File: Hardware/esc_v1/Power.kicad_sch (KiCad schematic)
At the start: 19 parts, among them U1 AZ1117CH-5.0TRG1, U2 AZ1117CH-3.3TRG1, U3 TPS5450DDAR

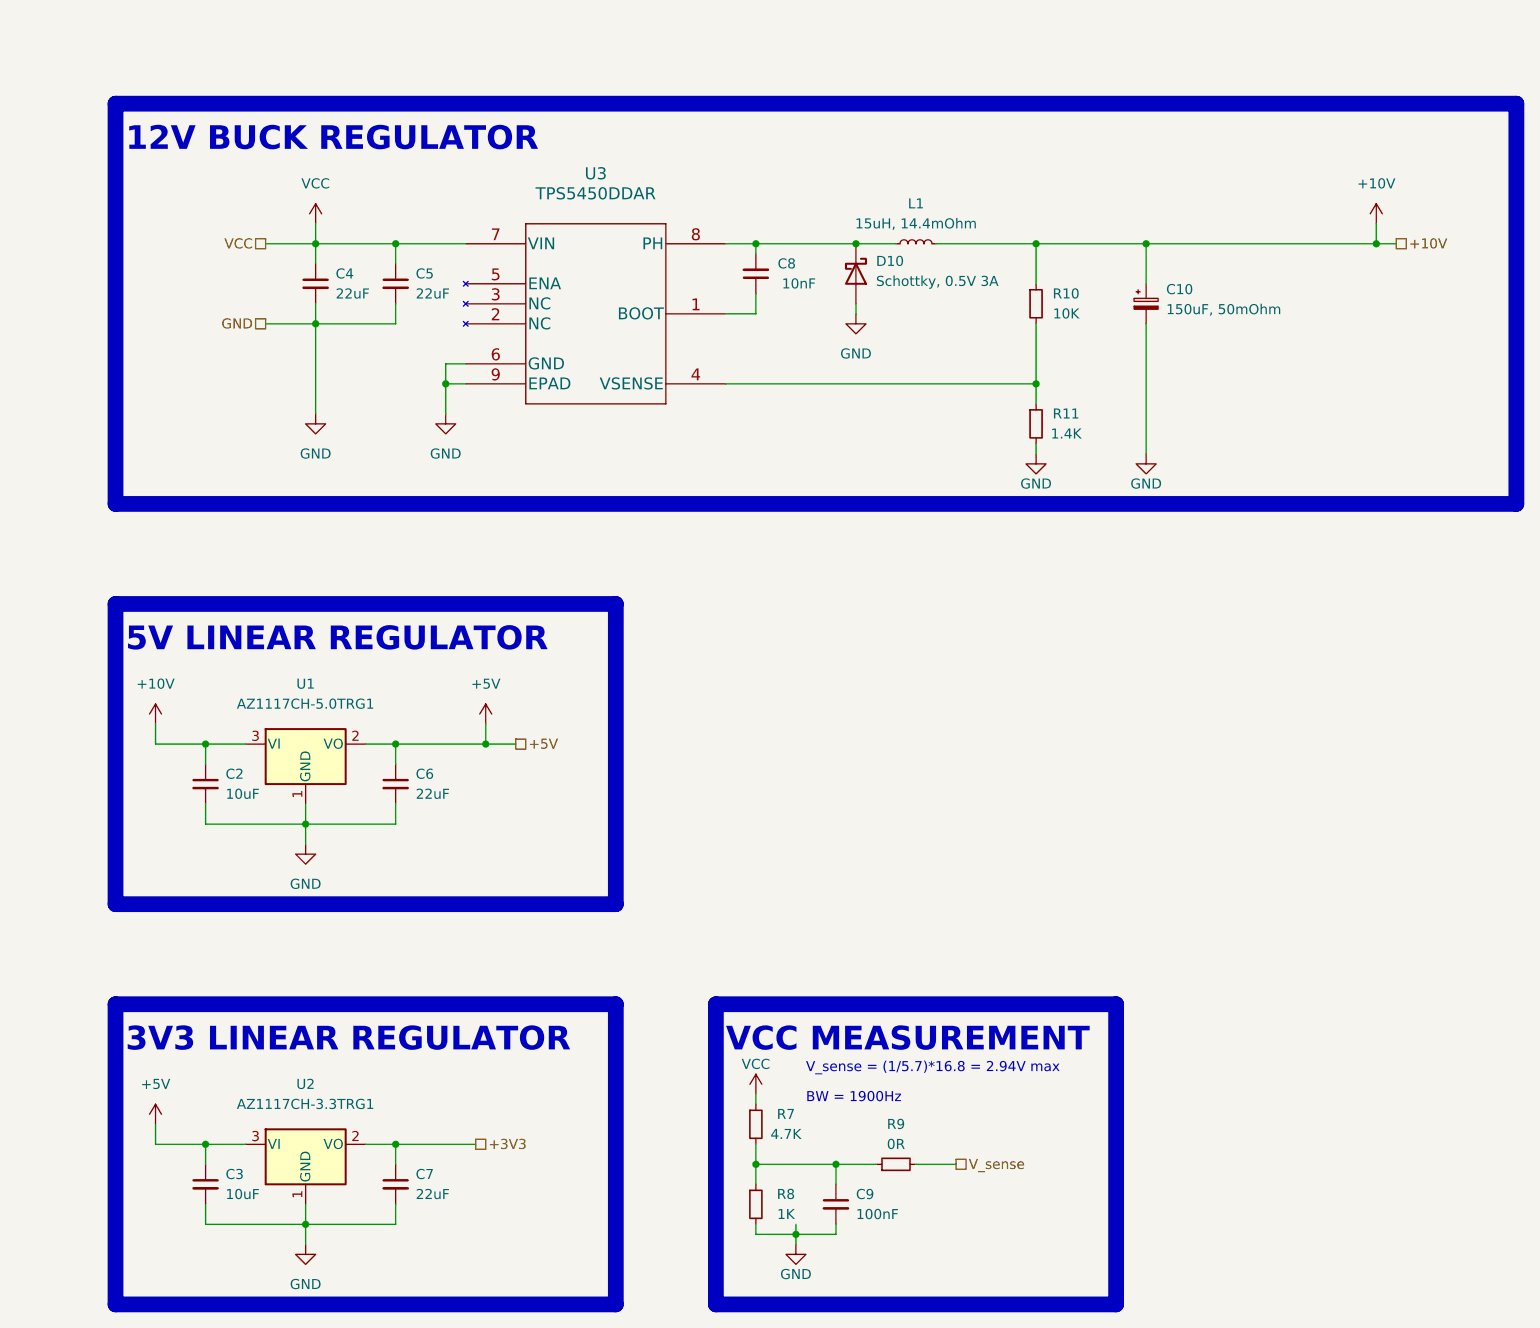
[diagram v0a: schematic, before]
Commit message: changed gate driver, removed 10V buck and 5V LDO, added 5V buck. Started on Layout
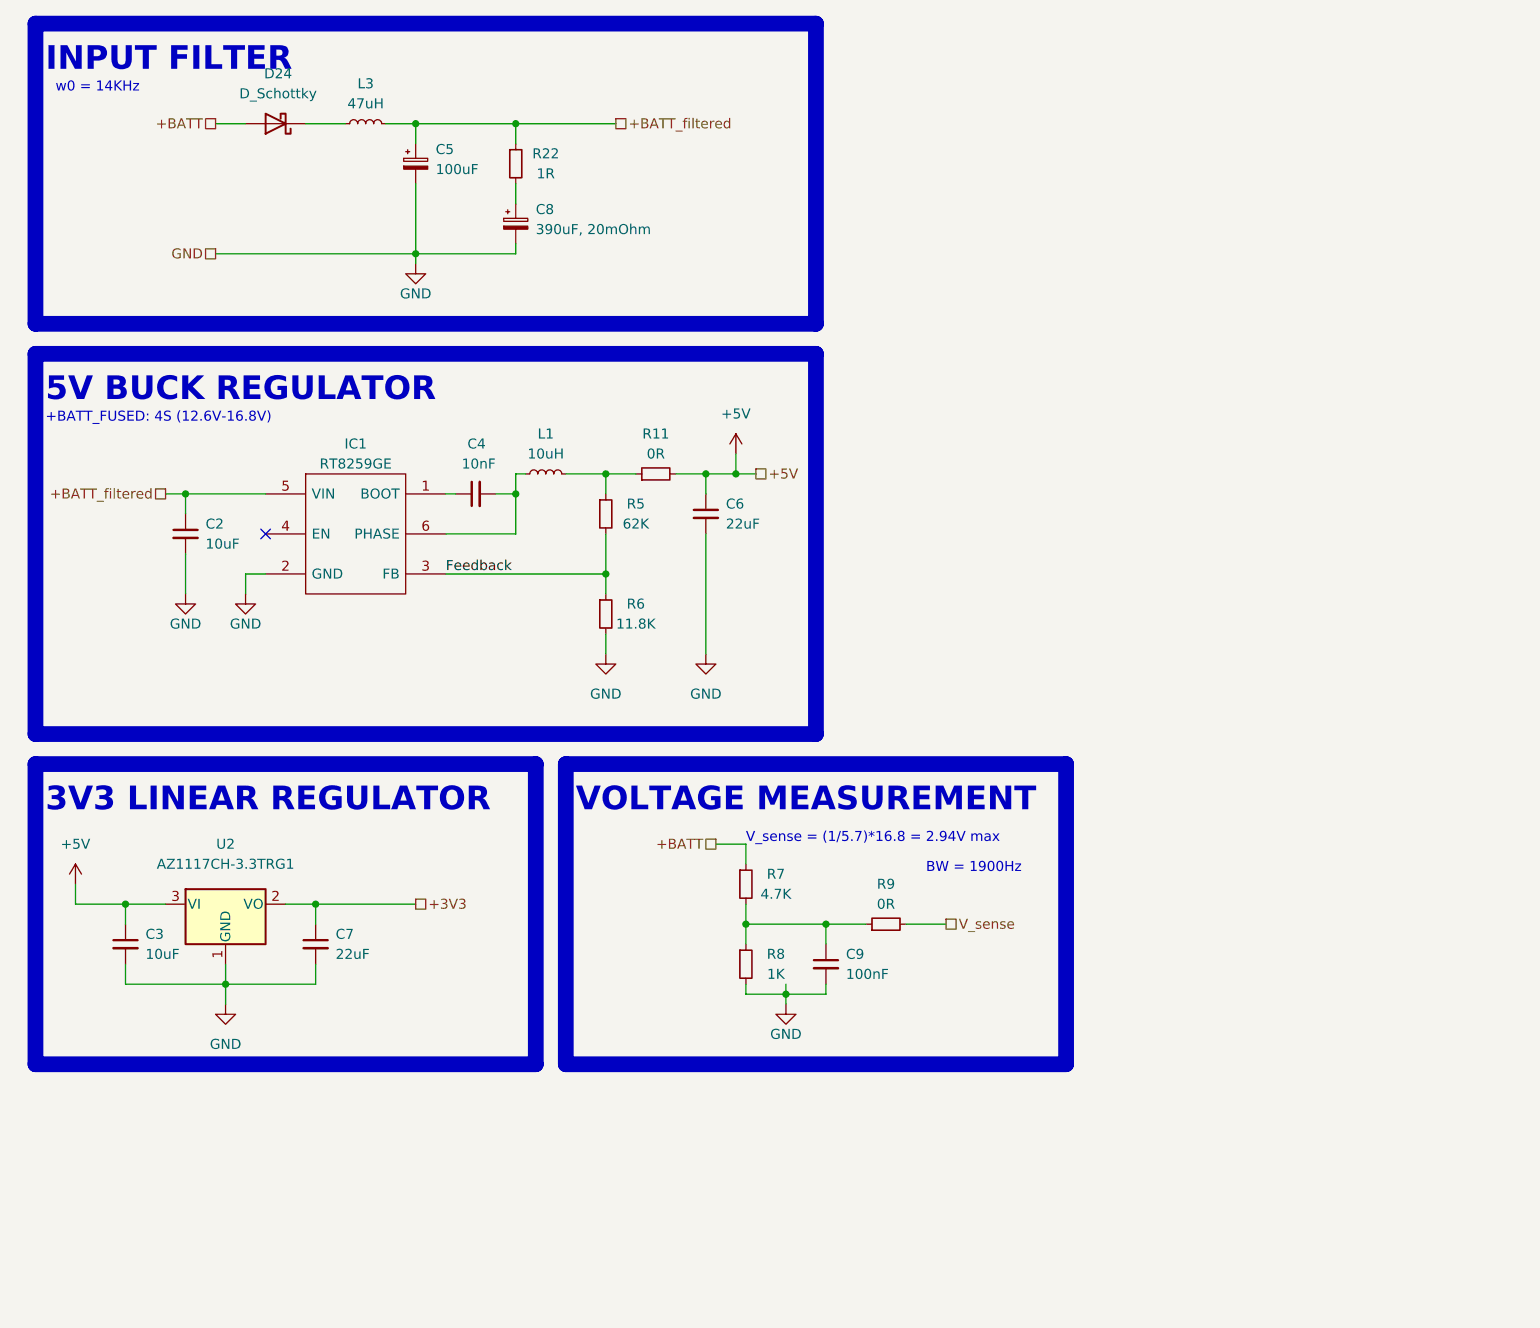
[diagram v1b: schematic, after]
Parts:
- removed C10: 150uF, 50mOhm, T510E107M025ATE050:T510E107M025AT E050, symbol Device:C_Polarized_Small
- removed C5: 22uF, Capacitor_SMD:C_0603_1608Metric, symbol Device:C_Small
- removed C8: 10nF, Capacitor_SMD:C_0603_1608Metric, symbol Device:C_Small
- removed D10: Schottky, 0.5V 3A, Diode_SMD:D_SMA, symbol Device:D_Schottky
- removed R10: 10K, Resistor_SMD:R_0603_1608Metric, symbol Device:R_Small
- removed U1: AZ1117CH-5.0TRG1, Package_TO_SOT_SMD:SOT-223-3_TabPin2, symbol Regulator_Linear:AZ1117-3.3
- removed U3: TPS5450DDAR, Package_SO:TI_SO-PowerPAD-8, symbol TPS5450:TPS5450DDAR
- added C5: 100uF, T510E107M025ATE050:T510E107M025AT E050, symbol Device:C_Polarized_Small
- added C8: 390uF, 20mOhm, Capacitor_SMD:C_Elec_8x10.2, symbol Device:C_Polarized_Small
- added D24: D_Schottky, Diode_SMD:D_SOD-123, symbol Device:D_Schottky
- added IC1: RT8259GE, Package_TO_SOT_SMD:SOT-23-6, symbol RT8259GE:RT8259GE
- added L3: 47uH, SRP1265A-470M:SRP1265A, symbol Device:L_Small
- added R22: 1R, Resistor_SMD:R_0603_1608Metric, symbol Device:R_Small
- added R5: 62K, Resistor_SMD:R_0603_1608Metric, symbol Device:R_Small
- added R6: 11.8K, Resistor_SMD:R_0603_1608Metric, symbol Device:R_Small
- C4: value 22uF -> 10nF
- C6, C7: footprint Capacitor_SMD:C_0603_1608Metric -> Capacitor_SMD:C_0805_2012Metric
- L1: value 15uH, 14.4mOhm -> 10uH; footprint IHLP6767GZER150M11:INDPM172172X700N -> 744025100:Wuerth_Elektronik-744025100-Manufacturer_Recommended; Part No IHLP6767GZER150M11 -> 744025100; Producer Vishay Dale -> Würth Elektronik
- R11: value 1.4K -> 0R
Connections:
- net +5V: now also R11.2
- net GND: now also C5.2, C8.2, IC1.2 (GND), R6.2; no longer C4.2, R11.2
- net at L1.1: now also C4.2, IC1.6 (PHASE)
- net at R11.1: now also L1.2, R5.1
- net +10V renamed +BATT_filtered
- net +BATT_filtered: now also C5.1, IC1.5 (VIN), L3.2, R22.1; no longer L1.2
- net VCC: no longer names the net of C4.1
- net VCC: now also IC1.1 (BOOT); no longer R7.1
- new net: D24.1 (K), L3.1
- new net: C8.1, R22.2
- new net +BATT: D24.2 (A), R7.1
- new net Feedback: IC1.3 (FB), R5.2, R6.1
- no-connect marks 0 -> 1
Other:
- note added: "+BATT_FUSED: 4S (12.6V-16.8V)"
- note added: "5V BUCK REGULATOR"
- note added: "INPUT FILTER"
- note added: "VOLTAGE MEASUREMENT"
- note added: "w0 = 14KHz"
- note removed: "12V BUCK REGULATOR"
- note removed: "5V LINEAR REGULATOR"
- note removed: "VCC MEASUREMENT"
- moved on the sheet: C3, C7, C9, R7, R8, R9, U2

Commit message: Continued on layout
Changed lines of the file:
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@@
     (pin "2")
   )
-  (symbol (lib_id "Device:C_Small") (at 26.67 132.08 0) (unit 1)
+  (symbol (lib_id "Device:C_Small") (at 26.67 132.08 0) (mirror y) (unit 1)
     (in_bom yes) (on_board yes)
-    (property "Reference" "C3" (id 0) (at 29.21 130.8162 0)
+    (property "Reference" "C3" (id 0) (at 24.13 130.8162 0)
       (effects (font (size 1.27 1.27)) (justify left))
     )
-    (property "Value" "10uF" (id 1) (at 29.21 133.3562 0)
+    (property "Value" "10uF" (id 1) (at 24.13 133.3562 0)
       (effects (font (size 1.27 1.27)) (justify left))
     )

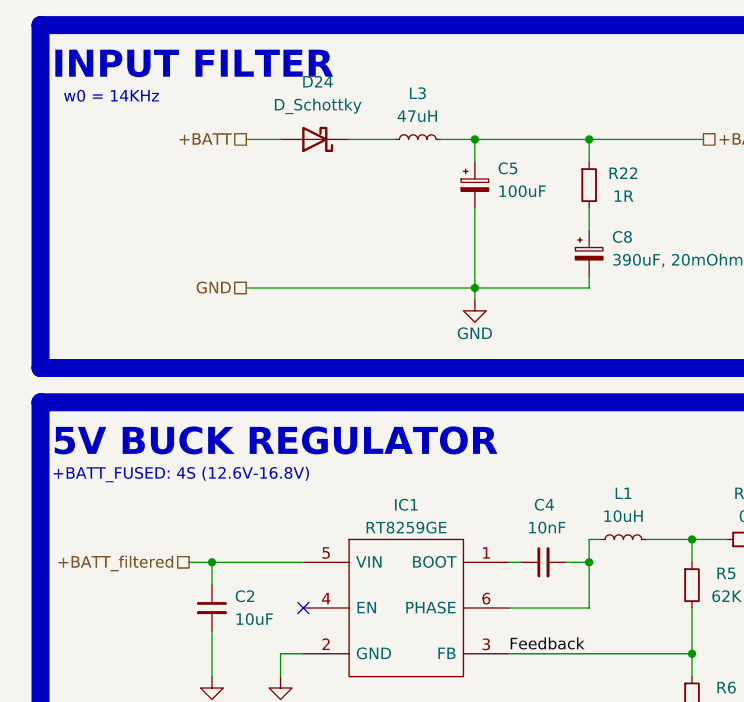
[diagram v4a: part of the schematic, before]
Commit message: Removed USB to serial chip and added serial connector. Finished layout, made production files and sent to production
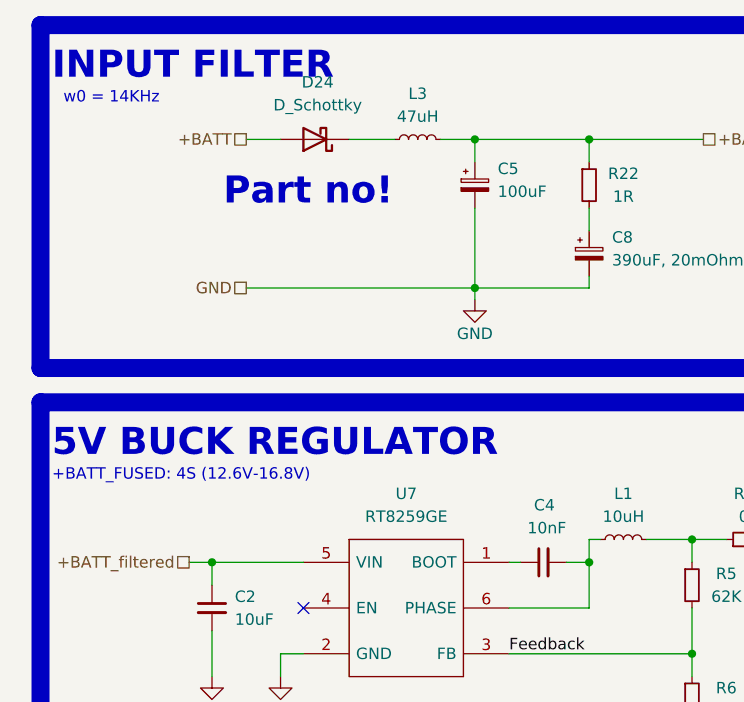
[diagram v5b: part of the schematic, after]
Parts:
- C5: Part no (none) -> T510E107M025ATE050; PartNo T510E107M025ATE050 -> (none)
- C8: Part no (none) -> APXG200ARA391MHA0G; PartNo APXG200ARA391MHA0G -> (none)
- D24: Io 1.5A -> 2A; Part no (none) -> MBR260HW; Producer (none) -> SMC Diode Solutions; Voltage rating 50V -> 60V
- L1: Manufacturer_Name (none) -> Würth Elektronik; Part No 744025100 -> (none); Part no (none) -> 744025100; Producer Würth Elektronik -> (none)
- L3: Manufacturer_Name (none) -> Bourns Inc.; Part No SRP1265A-470M -> (none); Part no (none) -> SRP1265A-470M; Producer Bourns Inc. -> (none)
- U2: Part no (none) -> AZ1117CH-3.3TRG1
- U7: renamed from IC1; Manufacturer_Part_Number RT8259GE -> (none); Part no (none) -> RT8259GE
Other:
- note added: "Part no!"
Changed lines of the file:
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@@
     (effects (font (size 1.27 1.27)) (justify left bottom))
+  )
+  (text "Part no!" (at 35.56 35.56 0)
+    (effects (font (size 3 3) (thickness 0.6) bold) (justify left bottom))
   )
   (text "5V BUCK REGULATOR" (at 16.51 63.5 0)
@@
       (effects (font (size 1.27 1.27)) hide)
     )
-    (property "Part no" "" (id 4) (at 45.72 27.94 90)
-      (effects (font (size 1.27 1.27)) hide)
-    )
-    (property "Producer" "" (id 5) (at 45.72 27.94 90)
-      (effects (font (size 1.27 1.27)) hide)
-    )
-    (property "Voltage rating" "50V" (id 6) (at 45.72 27.94 0)
-      (effects (font (size 1.27 1.27)) hide)
-    )
-    (property "Io" "1.5A" (id 7) (at 45.72 27.94 0)
+    (property "Part no" "MBR260HW" (id 4) (at 45.72 27.94 90)
+      (effects (font (size 1.27 1.27)) hide)
+    )
+    (property "Producer" "SMC Diode Solutions" (id 5) (at 45.72 27.94 90)
+      (effects (font (size 1.27 1.27)) hide)
+    )
+    (property "Voltage rating" "60V" (id 6) (at 45.72 27.94 0)
+      (effects (font (size 1.27 1.27)) hide)
+    )
+    (property "Io" "2A" (id 7) (at 45.72 27.94 0)
       (effects (font (size 1.27 1.27)) hide)
     )
@@
   (symbol (lib_id "RT8259GE:RT8259GE") (at 44.45 74.93 0) (unit 1)
     (in_bom yes) (on_board yes) (fields_autoplaced)
-    (property "Reference" "IC1" (id 0) (at 55.88 68.58 0))
-    (property "Value" "RT8259GE" (id 1) (at 55.88 71.12 0))
+    (property "Reference" "U7" (id 0) (at 55.88 67.31 0))
+    (property "Value" "RT8259GE" (id 1) (at 55.88 69.85 0))
     (property "Footprint" "Package_TO_SOT_SMD:SOT-23-6" (id 2) (at 71.12 72.39 0)
       (effects (font (size 1.27 1.27)) (justify left) hide)
@@
       (effects (font (size 1.27 1.27)) (justify left) hide)
     )
-    (property "Manufacturer_Part_Number" "RT8259GE" (id 7) (at 71.12 85.09 0)
+    (property "Part no" "RT8259GE" (id 7) (at 71.12 85.09 0)
       (effects (font (size 1.27 1.27)) (justify left) hide)
     )
@@
       (effects (font (size 1.27 1.27)) hide)
     )
-    (property "PartNo" "T510E107M025ATE050" (id 4) (at 63.5 33.02 0)
+    (property "Part no" "T510E107M025ATE050" (id 4) (at 63.5 33.02 0)
       (effects (font (size 1.27 1.27)) hide)
     )
@@
       (effects (font (size 1.27 1.27)) hide)
     )
-    (property "Part No" "744025100" (id 4) (at 80.01 72.39 90)
-      (effects (font (size 1.27 1.27)) hide)
-    )
-    (property "Producer" "Würth Elektronik" (id 5) (at 80.01 72.39 90)
+    (property "Part no" "744025100" (id 4) (at 80.01 72.39 90)
+      (effects (font (size 1.27 1.27)) hide)
+    )
+    (property "Manufacturer_Name" "Würth Elektronik" (id 5) (at 80.01 72.39 90)
       (effects (font (size 1.27 1.27)) hide)
     )
@@
       (effects (font (size 1.27 1.27)) hide)
     )
-    (property "PartNo" "APXG200ARA391MHA0G" (id 4) (at 76.2 40.64 0)
+    (property "Part no" "APXG200ARA391MHA0G" (id 4) (at 76.2 40.64 0)
       (effects (font (size 1.27 1.27)) hide)
     )
@@
       (effects (font (size 1.27 1.27)) hide)
     )
+    (property "Part no" "AZ1117CH-3.3TRG1" (id 4) (at 39.37 127 0)
+      (effects (font (size 1.27 1.27)) hide)
+    )
     (pin "1")
     (pin "2")
@@
       (effects (font (size 1.27 1.27)) hide)
     )
-    (property "Part No" "SRP1265A-470M" (id 4) (at 57.15 27.94 90)
-      (effects (font (size 1.27 1.27)) hide)
-    )
-    (property "Producer" "Bourns Inc." (id 5) (at 57.15 27.94 90)
-      (effects (font (size 1.27 1.27)) hide)
-    )
+    (property "Part no" "SRP1265A-470M" (id 4) (at 57.15 27.94 90)
+      (effects (font (size 1.27 1.27)) hide)
+    )
+    (property "Manufacturer_Name" "Bourns Inc." (id 5) (at 57.15 27.94 90)
+      (effects (font (size 1.27 1.27)) hide)
+    )
